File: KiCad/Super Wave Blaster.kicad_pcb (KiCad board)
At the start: 2 copper layers, 38 x 21.2 mm, 16 parts, among them J1 EIAJ_Input, J2 PCM5102_I2S, J3 PCM5102_Audio, J4 Power Input, J5 Audio_Out, J6 Power Input, U1 TLV73333PDBV, U2 CD74HCT14PWR, U3 SN74HC595PWR, U4 SN74LVC8T245PWR

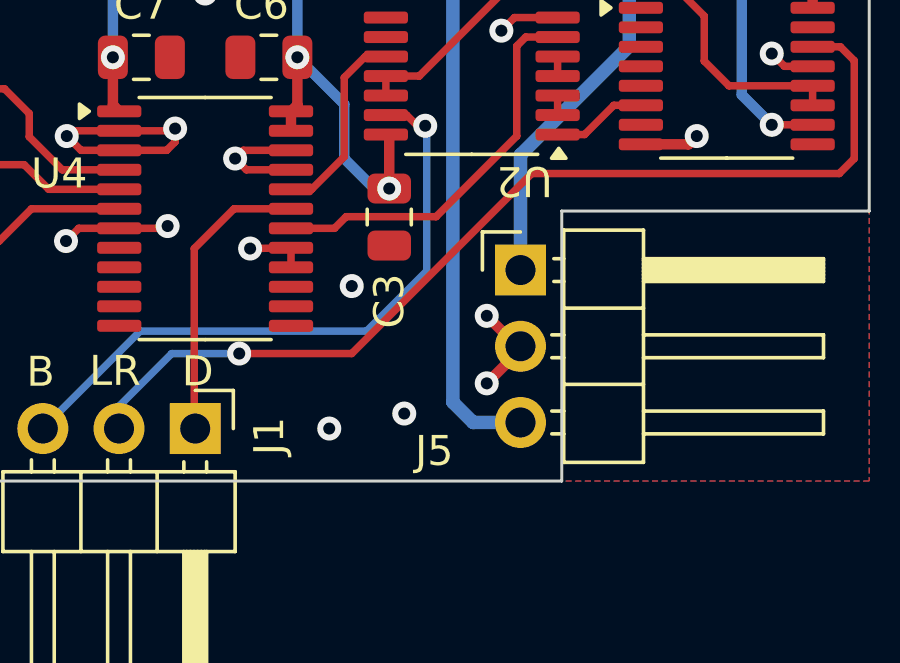
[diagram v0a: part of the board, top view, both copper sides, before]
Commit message: Add labels to audio headers
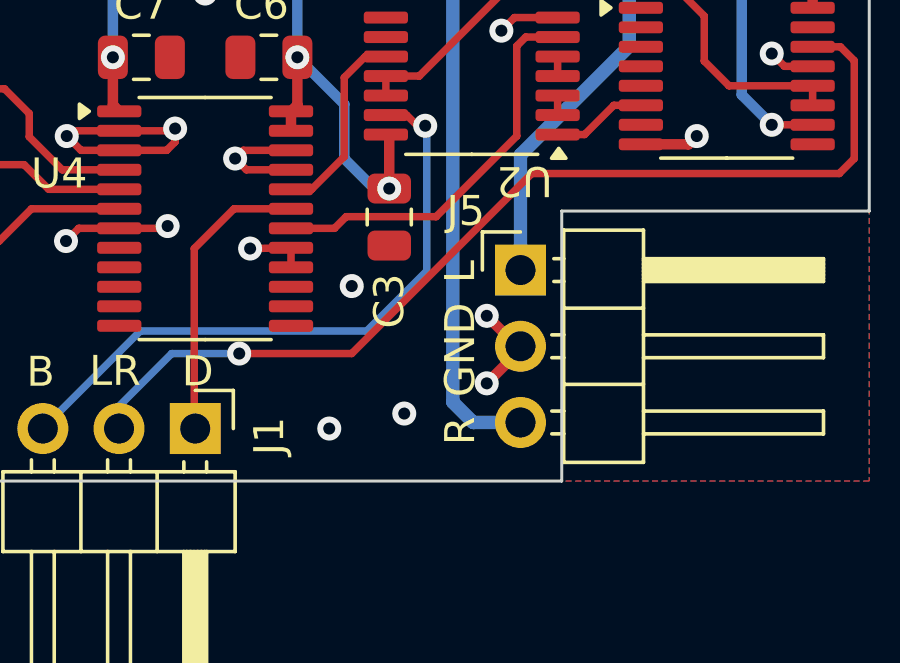
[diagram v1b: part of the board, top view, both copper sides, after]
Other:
- board text added: "L"
- board text added: "R"
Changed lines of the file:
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@@
 		(tags "Through hole angled pin header THT 1x03 2.54mm single row")
 		(property "Reference" "J5"
-			(at -2.875 6.0325 0)
+			(at -1.825 -1.9675 0)
 			(layer "F.SilkS")
 			(effects
@@
 		(layer "Edge.Cuts")
 	)
+	(gr_text "L\n"
+		(at 141.2 77.8 90)
+		(layer "B.SilkS")
+		(effects
+			(font
+				(size 1 1)
+				(thickness 0.15)
+			)
+			(justify left bottom mirror)
+		)
+	)
 	(gr_text "V1.0"
 		(at 153.5 75.5 0)
@@
 		)
 	)
+	(gr_text "GND"
+		(at 141.2 79 90)
+		(layer "B.SilkS")
+		(effects
+			(font
+				(size 1 1)
+				(thickness 0.15)
+			)
+			(justify left bottom mirror)
+		)
+	)
 	(gr_text "LRCK"
 		(at 128.532925 82 -90)
@@
 		)
 	)
+	(gr_text "R"
+		(at 141.2 82.6 90)
+		(layer "B.SilkS")
+		(effects
+			(font
+				(size 1 1)
+				(thickness 0.15)
+			)
+			(justify left bottom mirror)
+		)
+	)
 	(gr_text "-"
 		(at 119.463513 81.804741 0)
@@
 		)
 	)
+	(gr_text "R"
+		(at 141.2 83.8 90)
+		(layer "F.SilkS")
+		(effects
+			(font
+				(size 1 1)
+				(thickness 0.15)
+			)
+			(justify left bottom)
+		)
+	)
 	(gr_text "D"
 		(at 131.336252 81.931167 0)
@@
 		)
 	)
+	(gr_text "L\n"
+		(at 141.2 78.4 90)
+		(layer "F.SilkS")
+		(effects
+			(font
+				(size 1 1)
+				(thickness 0.15)
+			)
+			(justify left bottom)
+		)
+	)
 	(gr_text "GND"
 		(at 121.5 69.25 270)
@@
 		)
 	)
+	(gr_text "GND"
+		(at 141.2 82.2 90)
+		(layer "F.SilkS")
+		(effects
+			(font
+				(size 1 1)
+				(thickness 0.15)
+			)
+			(justify left bottom)
+		)
+	)
 	(gr_text "B"
 		(at 126.156591 81.946672 0)
@@
 		)
 	)
+	(group ""
+		(members "42034cbc-0ffb-4fd6-b72a-2bd17f854c85" "5ac7d301-2f4e-4365-9d49-d97b426bce7d")
+	)
 )

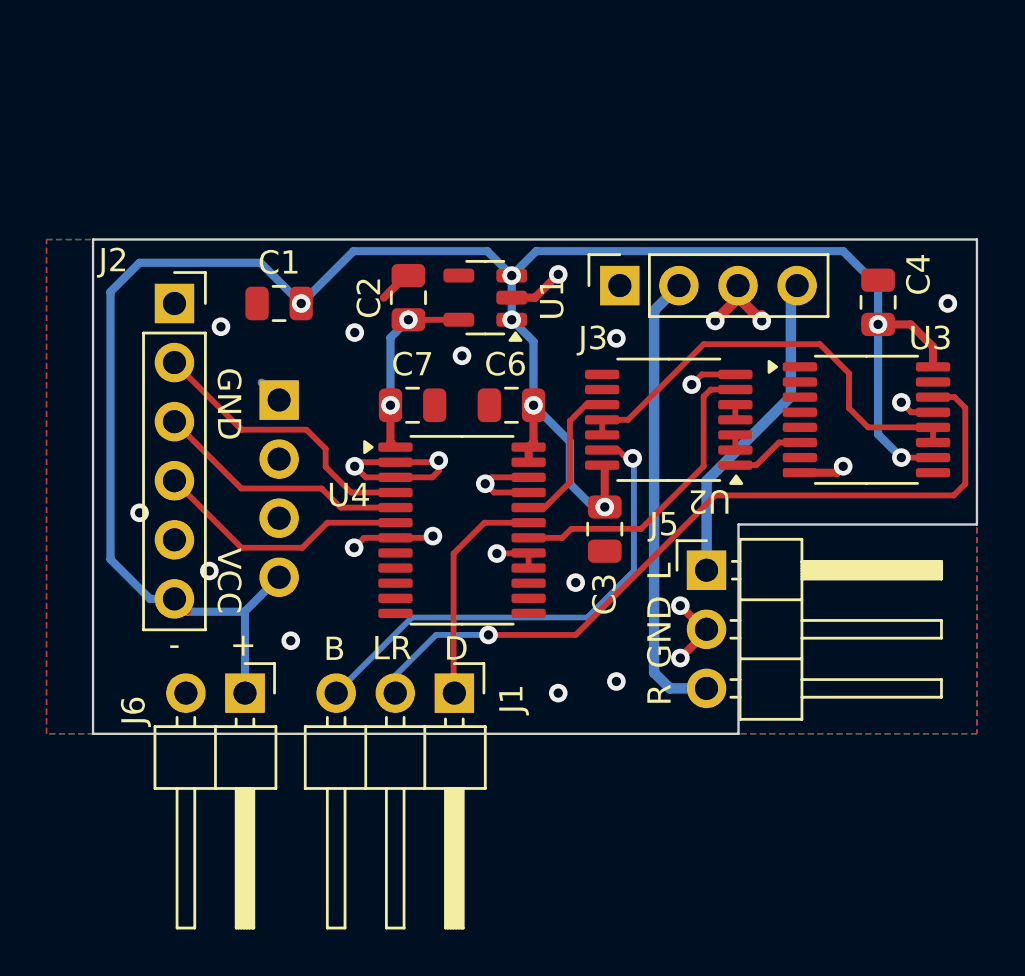
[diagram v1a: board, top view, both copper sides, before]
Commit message: Cleanup ground plane
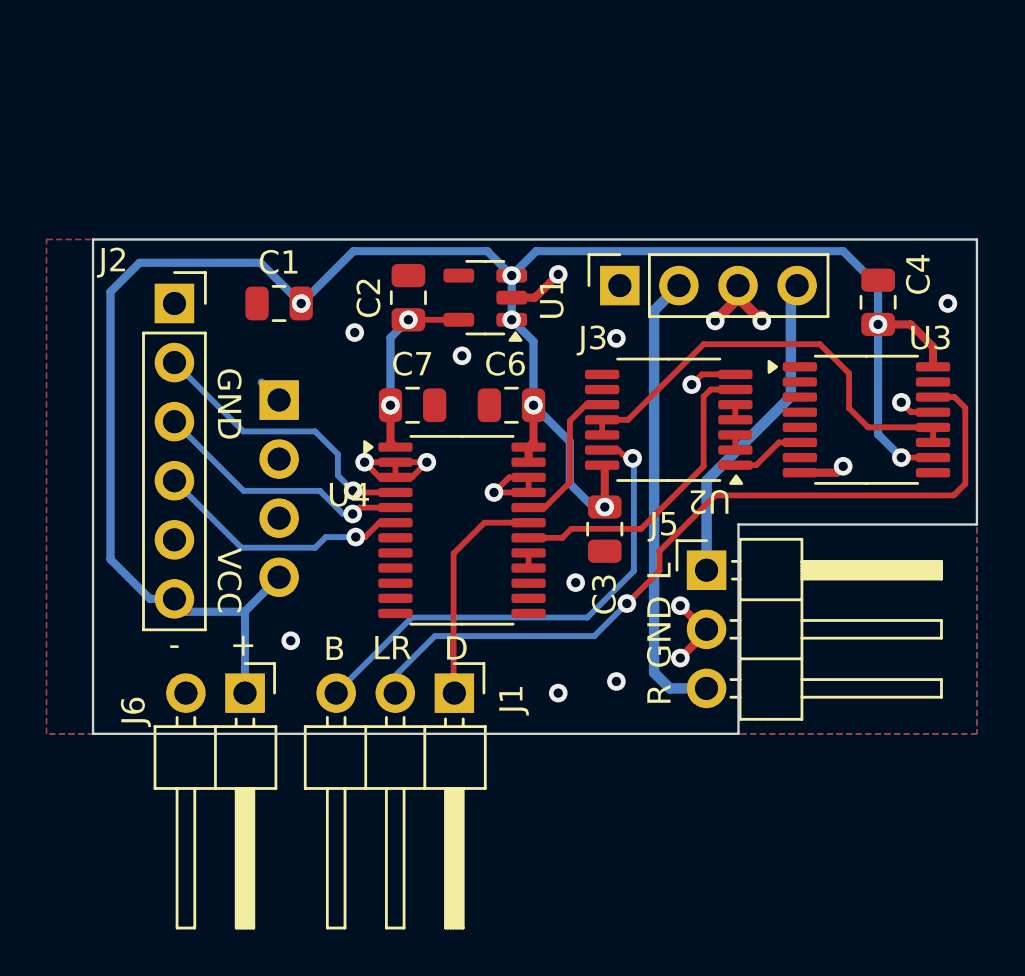
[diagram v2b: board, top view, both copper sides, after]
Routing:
- net GND: track 37.0 -> 29.0 mm, vias 25 -> 19
- net BCK_VDD: track 12.3 -> 12.5 mm, vias 0 -> 1
- net DIN_VDD: track 11.0 -> 11.3 mm, vias 0 -> 1
- net LRCK_VDD: vias 0 -> 1

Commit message: Revision v1.1
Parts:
- added C5: 1uf, Capacitor_SMD:C_0805_2012Metric, F.Cu at (146.7, 66.2)
- added C8: 1uf, Capacitor_SMD:C_0805_2012Metric, F.Cu at (137.3, 68.8)
- added J7: Audio Out, Connector_PinHeader_2.54mm:PinHeader_1x02_P2.54mm_Horizontal, F.Cu at (149.8, 65.6)
- added R1: 24k, Resistor_SMD:R_0805_2012Metric, F.Cu at (150.1, 68.7)
- added R2: 24k, Resistor_SMD:R_0805_2012Metric, F.Cu at (133.0, 66.2)
- J5: value Audio_Out -> Audio_Jack
- moved U1 8.38 mm to (124.7, 66.5), turned to 0 degrees
- moved C4 5.86 mm to (152.6, 71.7), turned to -90 degrees
- moved C1 4.24 mm to (120.1, 67.3), turned to -90 degrees
- moved J2 2.91 mm to (116.8, 66.6)
- moved J3 2.91 mm to (136.0, 65.9)
- moved U3 2.52 mm to (147.3, 72.7)
- moved C3 2.31 mm to (136.3, 77.5)
- moved U2 2.18 mm to (139.2, 72.7)
- moved C2 1.73 mm to (128.1, 66.0)
- moved C6 1.40 mm to (132.8, 71.0)
- moved C7 1.40 mm to (128.6, 71.0)
- moved U4 1.40 mm to (130.7, 76.4)
- moved J5 0.50 mm to (142.1, 78.0)
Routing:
- net Net-(J7-Pin_1): track 0.00 -> 18.3 mm, vias 0 -> 1
- net VCC: track 91.0 -> 96.4 mm, vias 7 -> 8
- net LRCK_VDD: track 11.1 -> 15.9 mm
- net DIN_VDD: track 11.3 -> 15.7 mm
- net BCK_EIAJ: track 21.3 -> 16.9 mm
- net BCK_VDD: track 12.5 -> 16.8 mm
- net Net-(C8-Pad2): track 0.00 -> 4.09 mm, vias 0 -> 2
- net GND: track 29.0 -> 25.1 mm, vias 19 -> 23
- net Net-(J7-Pin_2): track 0.00 -> 3.57 mm, vias 0 -> 1
- net AUDIO_L: track 13.8 -> 17.1 mm, vias 0 -> 1
- net Net-(C5-Pad2): track 0.00 -> 3.12 mm, vias 0 -> 2
- net BCK_INV: track 19.2 -> 21.2 mm
- net LRCK_EIAJ: track 34.0 -> 32.2 mm
- net DIN_EIAJ: track 9.79 -> 8.48 mm, vias 0 -> 1
- net VDD: track 8.16 -> 8.96 mm, vias 2 -> 3
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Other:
- board size 38 x 21.2 mm -> 40 x 21.2 mm
- board text added: "V1.1"
- board text removed: "V1.0"
